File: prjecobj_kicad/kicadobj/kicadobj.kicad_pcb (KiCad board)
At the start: 2 copper layers, 34 parts, among them J1 MAX9812_Con_Pin_0103_V, J2 Conn_01x05, J3 Conn_01x05, J4 PCM1808_Con_Pin_0103_V, U5 PJ-342B

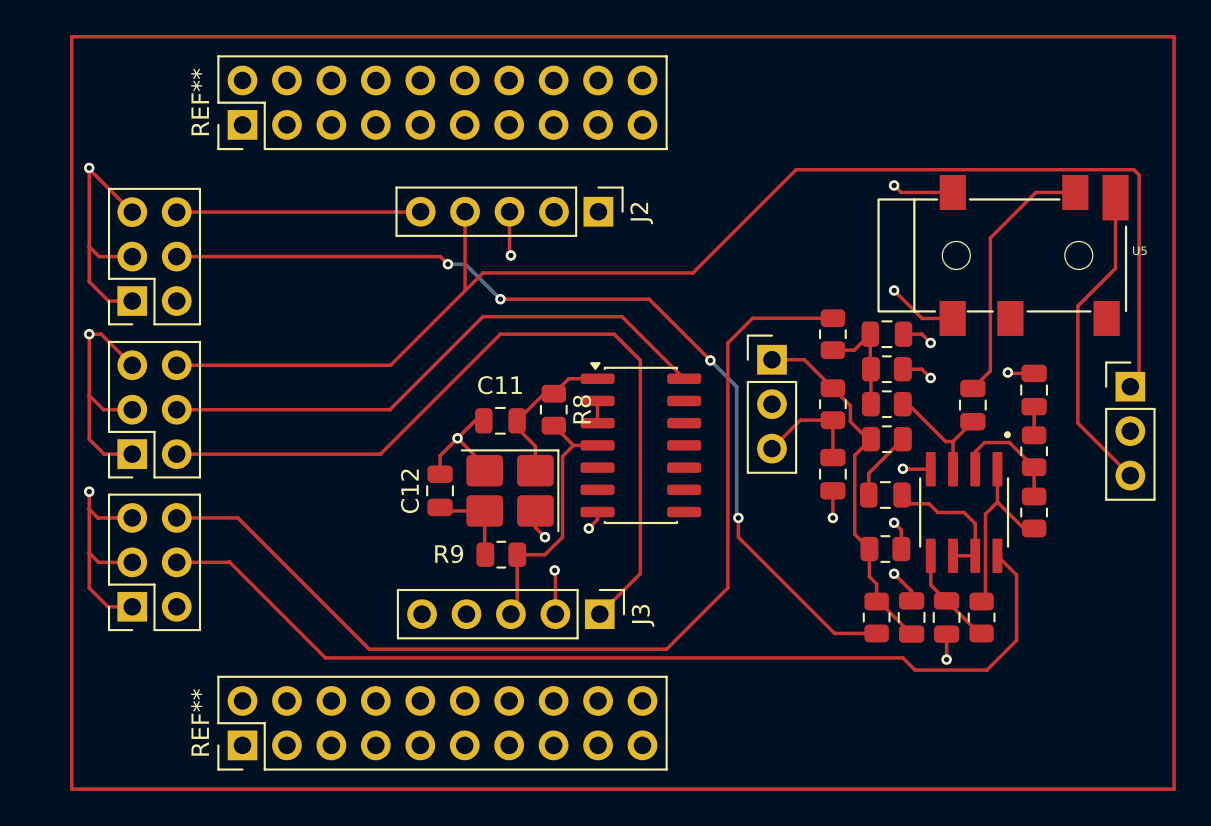
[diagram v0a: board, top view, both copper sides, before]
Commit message: feat(kicad): update connector from 1x5 to 1x6 with adding net
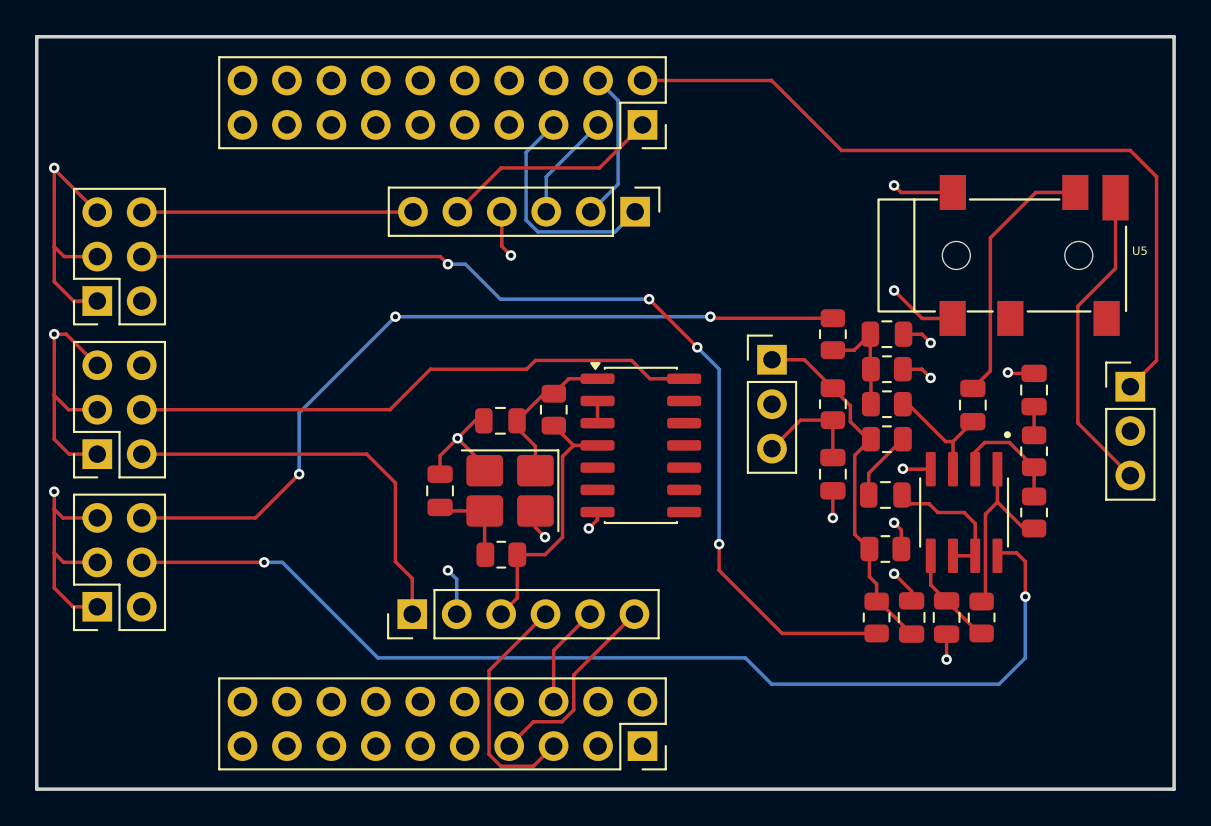
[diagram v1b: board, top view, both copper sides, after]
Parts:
- removed the REF** at (171.8, 144.0)
- removed the REF** at (171.8, 108.5)
- added J5: Conn_01x06, Connector_PinHeader_2.54mm:PinHeader_1x06_P2.54mm_Vertical, F.Cu at (194.2, 113.5)
- added J6: Conn_02x10_Top_Bottom, Connector_PinSocket_2.54mm:PinSocket_2x10_P2.54mm_Vertical, F.Cu at (194.6, 144.0)
- J2: value Conn_01x05 -> Conn_01x06; footprint Connector_PinHeader_2.54mm:PinHeader_1x05_P2.54mm_Vertical -> Connector_PinHeader_2.54mm:PinHeader_1x06_P2.54mm_Vertical
- J3: value Conn_01x05 -> Conn_02x10_Top_Bottom; footprint Connector_PinHeader_2.54mm:PinHeader_1x05_P2.54mm_Vertical -> Connector_PinSocket_2.54mm:PinSocket_2x10_P2.54mm_Vertical
- moved J3 28.1 mm to (194.6, 108.5)
- moved J2 25.3 mm to (181.5, 136.5), turned to 90 degrees
- moved REF** 2.00 mm to (163.5, 136.1)
- moved REF** 2.00 mm to (163.5, 118.6)
- moved REF** 2.00 mm to (163.5, 127.4)
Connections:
- INVBUF1 pad 4: Net-(J3-Pin_3) -> Net-(J2-Pin_3)
- J2 pad 1: unconnected-(J2-Pin_1-Pad1) -> 3.3V
- J2 pad 2: unconnected-(J2-Pin_2-Pad2) -> GND
- J2 pad 3: GND -> Net-(J2-Pin_3)
- J2 pad 4: 3.3V -> /LRC
- J2 pad 5: 5V -> /OUT
- J3 pad 2: GND -> 3.3V
- J3 pad 3: Net-(J3-Pin_3) -> /MD0
- J3 pad 4: unconnected-(J3-Pin_4-Pad4) -> /MD1
- J3 pad 5: unconnected-(J3-Pin_5-Pad5) -> /PMT
- R8 pad 2: Net-(J3-Pin_3) -> Net-(J2-Pin_3)
- R9 pad 2: Net-(J3-Pin_3) -> Net-(J2-Pin_3)
- REF** pad 2: 12V -> (no net)
- REF** pad 2: 5V -> (no net)
- REF** pad 6: 3.3V -> (no net)
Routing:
- net 3.3V: track 154.7 -> 112.6 mm
- net Net-(J2-Pin_3): track 0.00 -> 15.3 mm
- net Net-(J3-Pin_3): track 15.0 -> 0.00 mm
- net /LRC: track 0.00 -> 13.8 mm
- net /PMT: track 0.00 -> 13.1 mm
- net /BCK: track 0.00 -> 11.5 mm
- net /MD1: track 0.00 -> 8.63 mm
- net /MD0: track 0.00 -> 6.19 mm
- net /OUT: track 0.00 -> 5.86 mm
- net 5V: track 67.9 -> 73.6 mm
- net 12V: track 113.2 -> 107.7 mm, vias 0 -> 5
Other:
- board outline added: 65 x 43 mm
